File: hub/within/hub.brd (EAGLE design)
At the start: 28.2 x 26 mm, 5 parts

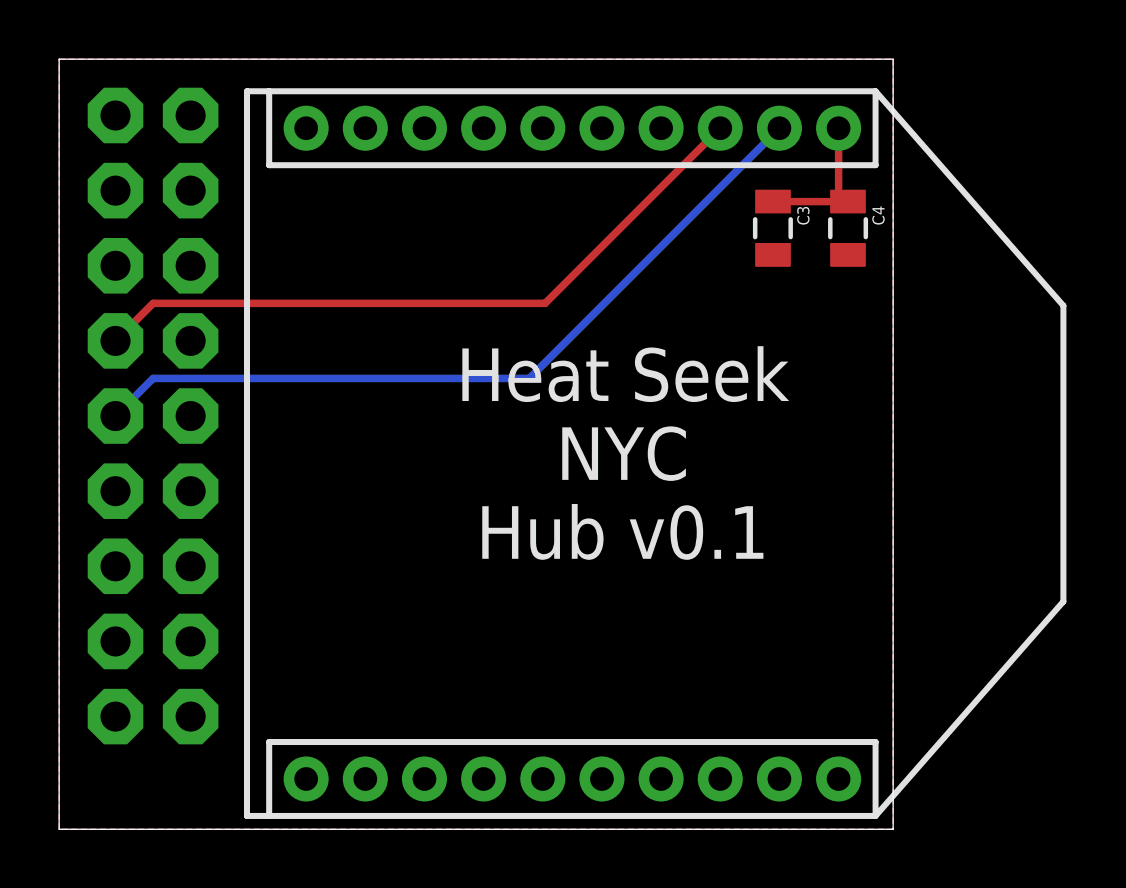
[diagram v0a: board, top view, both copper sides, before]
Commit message: tighter fit, turns out XBee fits perfectly on 1" wide board
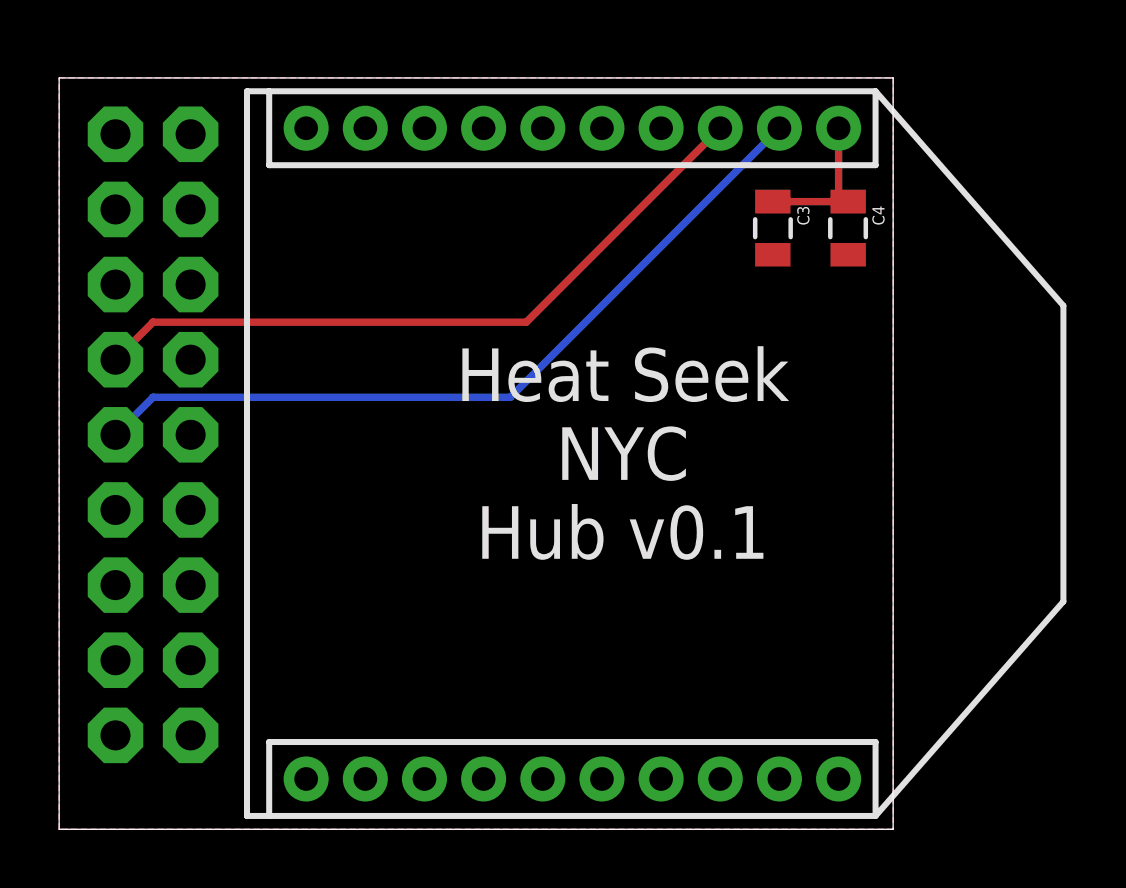
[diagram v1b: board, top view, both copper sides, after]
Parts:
- moved Rπ 0.63 mm to (3.17, 13.3)
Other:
- board size 28.2 x 26 mm -> 28.2 x 25.4 mm
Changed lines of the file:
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@@
 <plain>
 <wire x1="0" y1="0" x2="28.194" y2="0" width="0" layer="20"/>
-<wire x1="28.194" y1="0" x2="28.194" y2="26.035" width="0" layer="20"/>
-<wire x1="28.194" y1="26.035" x2="0" y2="26.035" width="0" layer="20"/>
-<wire x1="0" y1="26.035" x2="0" y2="0" width="0" layer="20"/>
+<wire x1="28.194" y1="0" x2="28.194" y2="25.4" width="0" layer="20"/>
+<wire x1="28.194" y1="25.4" x2="0" y2="25.4" width="0" layer="20"/>
+<wire x1="0" y1="25.4" x2="0" y2="0" width="0" layer="20"/>
 <text x="21.59" y="36.83" size="1.778" layer="51" ratio="15">Harold Cooper</text>
 <text x="19.05" y="12.7" size="1.778" layer="21" font="vector" ratio="15" align="center">Heat Seek
@@
 <elements>
 <element name="FRAME1" library="SparkFun-Aesthetics" package="CREATIVE_COMMONS" value="FRAME-LETTER" x="-6.35" y="36.83"/>
-<element name="Rπ" library="hrldcpr" package="2X9_NOSILK" value="M9X2" x="3.175" y="13.97" rot="MR270"/>
+<element name="Rπ" library="hrldcpr" package="2X9_NOSILK" value="M9X2" x="3.175" y="13.335" rot="MR270"/>
 <element name="XB24" library="hrldcpr" package="XBEE-1" value="XBEE-1XBEE-1" x="6.35" y="12.7" rot="R270"/>
 <element name="C3" library="SparkFun-Capacitors" package="0805" value="1µF" x="24.13" y="20.32" rot="R270"/>
@@
 <polygon width="0.3048" layer="1" isolate="0.3048">
 <vertex x="0" y="0"/>
-<vertex x="0" y="26.035"/>
-<vertex x="28.194" y="26.035"/>
+<vertex x="0" y="25.4"/>
+<vertex x="28.194" y="25.4"/>
 <vertex x="28.194" y="0"/>
 </polygon>
@@
 <polygon width="0.3048" layer="16" isolate="0.3048">
 <vertex x="0" y="0"/>
-<vertex x="0" y="26.035"/>
-<vertex x="28.194" y="26.035"/>
+<vertex x="0" y="25.4"/>
+<vertex x="28.194" y="25.4"/>
 <vertex x="28.194" y="0"/>
 </polygon>
@@
 <contactref element="Rπ" pad="8"/>
 <contactref element="XB24" pad="3"/>
-<wire x1="1.905" y1="16.51" x2="3.175" y2="17.78" width="0.254" layer="1"/>
-<wire x1="3.175" y1="17.78" x2="16.43" y2="17.78" width="0.254" layer="1"/>
-<wire x1="16.43" y1="17.78" x2="22.35" y2="23.7" width="0.254" layer="1"/>
+<wire x1="1.905" y1="15.875" x2="3.175" y2="17.145" width="0.254" layer="1"/>
+<wire x1="3.175" y1="17.145" x2="15.795" y2="17.145" width="0.254" layer="1"/>
+<wire x1="15.795" y1="17.145" x2="22.35" y2="23.7" width="0.254" layer="1"/>
 </signal>
 <signal name="N$1">
 <contactref element="XB24" pad="2"/>
-<wire x1="3.175" y1="15.24" x2="15.89" y2="15.24" width="0.254" layer="16"/>
-<wire x1="15.89" y1="15.24" x2="24.35" y2="23.7" width="0.254" layer="16"/>
 <contactref element="Rπ" pad="10"/>
-<wire x1="1.905" y1="13.97" x2="3.175" y2="15.24" width="0.254" layer="16"/>
+<wire x1="1.905" y1="13.335" x2="3.175" y2="14.605" width="0.254" layer="16"/>
+<wire x1="3.175" y1="14.605" x2="15.255" y2="14.605" width="0.254" layer="16"/>
+<wire x1="15.255" y1="14.605" x2="24.35" y2="23.7" width="0.254" layer="16"/>
 </signal>
 </signals>
